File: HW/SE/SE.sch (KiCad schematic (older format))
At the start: 17 parts, among them J1 Conn_01x03_Female, SW1 SW_Push, SW2 Reset, U1 ESP32-WROOM-32, U2 NHD-0420H1Z, U3 NHD-0420H1Z, U4 PCF8574

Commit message: AJustes Dsiplay
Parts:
- removed J1: Conn_01x03_Female, symbol Connector:Conn_01x03_Female
- added C1: 4.7u, symbol Device:C
- added J2: USB_B_Micro, symbol Connector:USB_B_Micro
- added J?: Conn_01x03_Female, symbol Connector:Conn_01x03_Female
- added Q1, Q2: BSS138, Package_TO_SOT_SMD:SOT-23, symbol Transistor_FET:BSS138
- added R6, R7: 10k, symbol Device:R
- added R8: 330, symbol Device:R
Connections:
- net 3.33v: now also Q1.1 (G), Q2.1 (G), R6.2, R7.2
- net 5v: now also C1.1, J2.1 (VBUS), R8.1
- net GND: now reaches D1.1 (K), R5.1, R6.1, R7.1, RV1.3, SW1.2, SW2.2, U1.1 (GND), U1.15 (GND), U1.38 (GND), U1.39 (GND), U2.1 (VSS), U3.1 (VSS), U4.8 (VSS)
- net GND: now also U2.16 (K), U3.16 (K), C1.2, J2.5 (GND), J?.3 (Pin_3)
- net at R4.2, U4.15 (SDA): now also Q2.3 (D); no longer U1.33 (IO21)
- net at U1.34 (RXD0/IO3): now also J?.2 (Pin_2)
- net at U1.35 (TXD0/IO1): now also J?.1 (Pin_1)
- net at R3.2, U4.14 (SCL): now also Q1.3 (D); no longer U1.36 (IO22)
- net at U2.15 (A): now also U3.15 (A), R8.2
- new net SCL: Q1.2 (S), R6.1, U1.36 (IO22)
- new net SDA: Q2.2 (S), R7.1, U1.33 (IO21)
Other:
- moved on the sheet: D1, R1, R2, R3, R4, R5, R6, R7, RV1, SW1, SW2, U1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

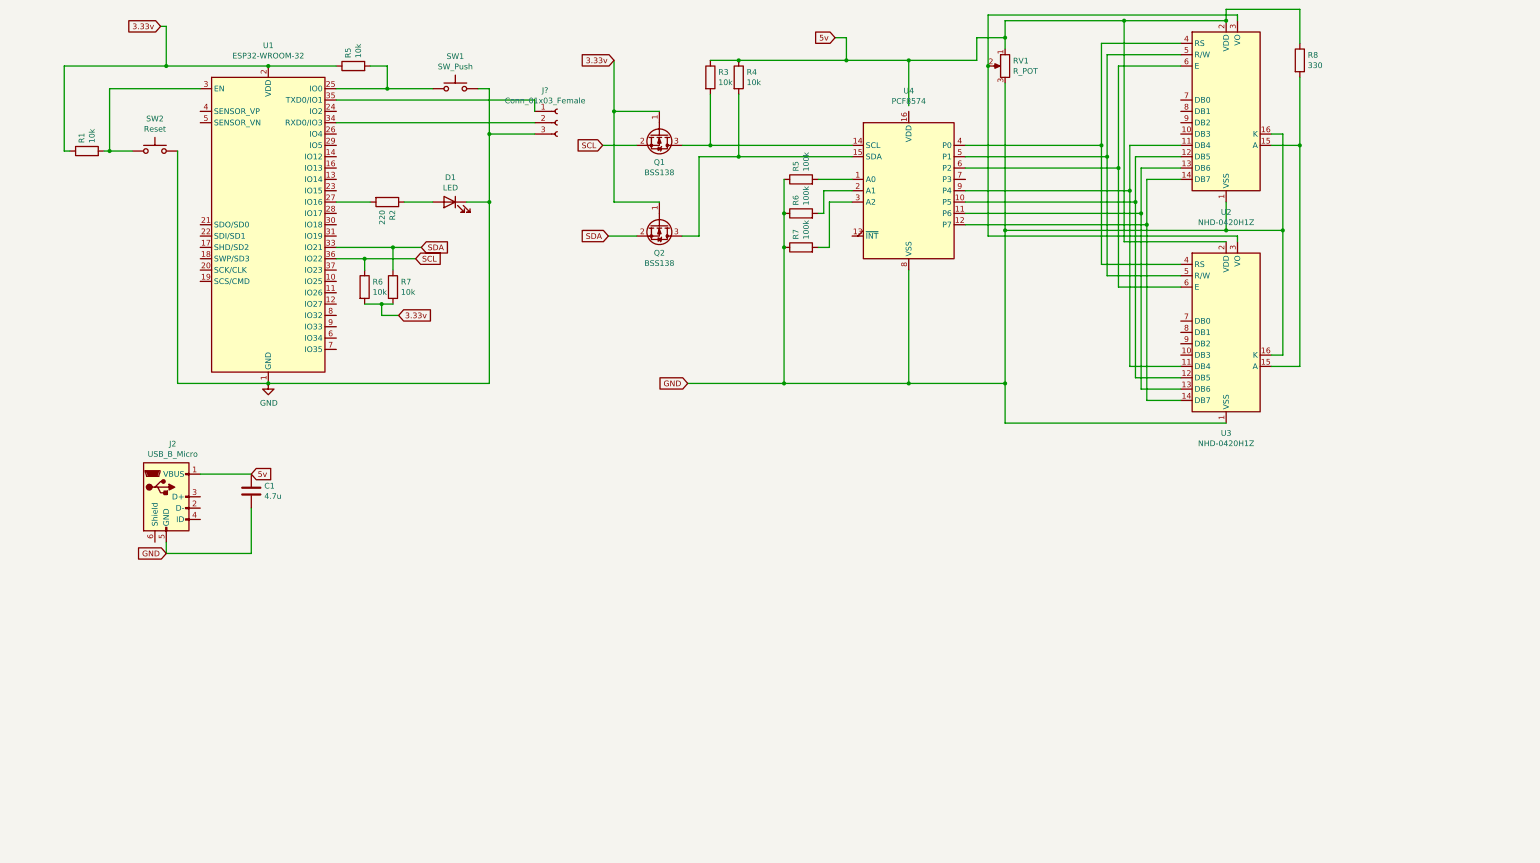
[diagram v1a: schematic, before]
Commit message: Control REle y entrada sensnores
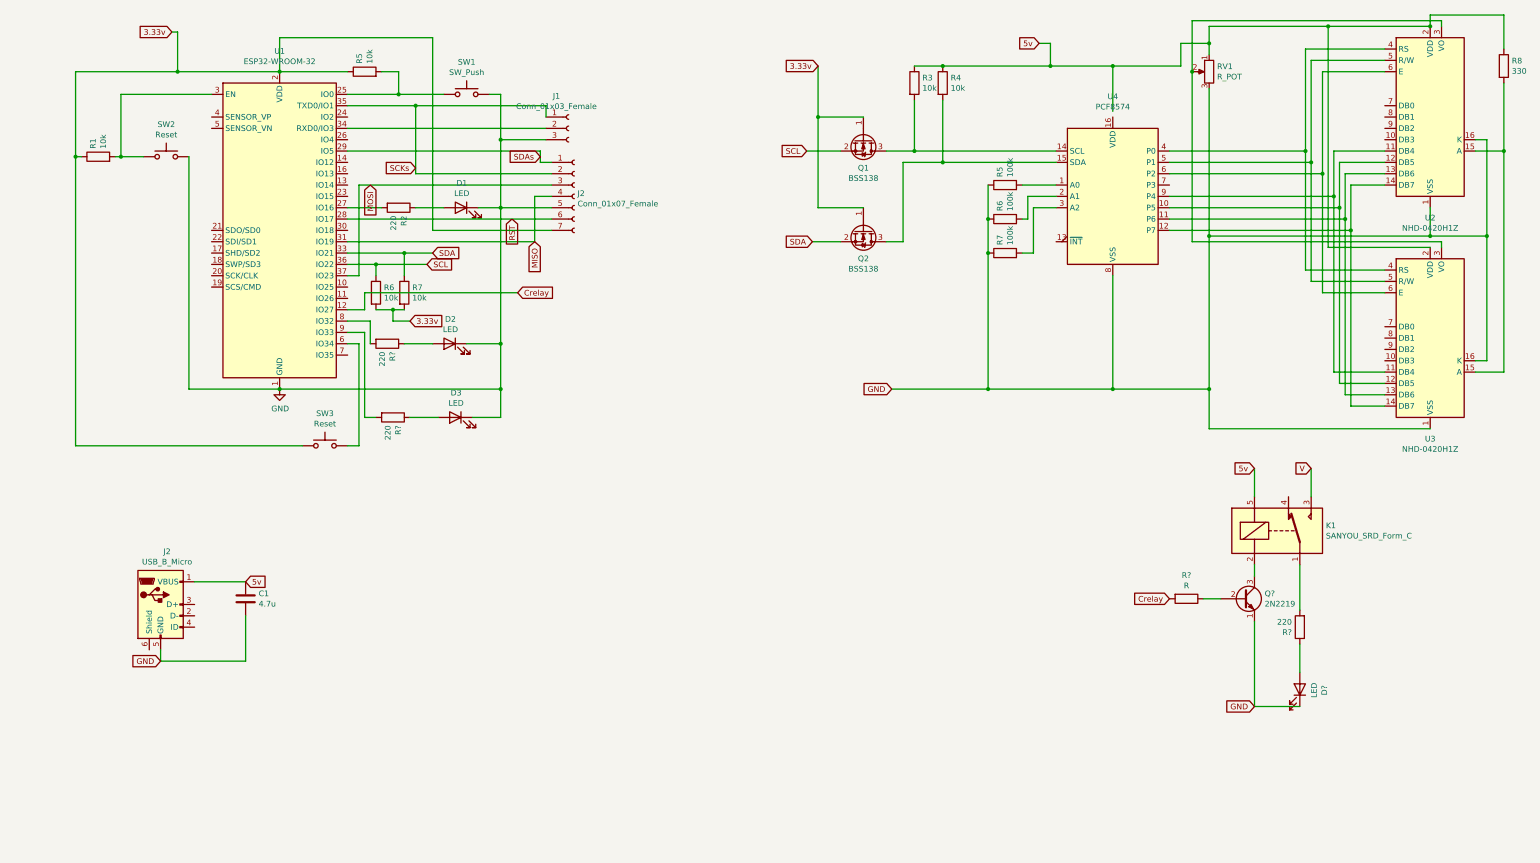
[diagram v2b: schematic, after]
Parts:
- added D2, D3, D?: LED, symbol Device:LED
- added J2: Conn_01x07_Female, symbol Connector:Conn_01x07_Female
- added K1: SANYOU_SRD_Form_C, Relay_THT:Relay_SPDT_SANYOU_SRD_Series_Form_C, symbol Relay:SANYOU_SRD_Form_C
- added Q?: 2N2219, Package_TO_SOT_THT:TO-39-3, symbol Transistor_BJT:2N2219
- added R? (x3): 220, symbol Device:R
- added R?: R, symbol Device:R
- added SW3: Reset, symbol Switch:SW_Push
- gave numbers to parts that had none: 1
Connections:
- net 3.33v: now also J2.7 (Pin_7), SW3.1
- net 5v: now also K1.5
- net GND: now also D2.1 (K), D3.1 (K), D?.1 (K), J2.5 (Pin_5), Q?.1 (E)
- net Crelay: now reaches U1.12 (IO27)
- net Crelay: now also R?.2
- net RST: now reaches U1.28 (IO17)
- net RST: now also J2.6 (Pin_6)
- net SDAs: now reaches U1.29 (IO5)
- net SDAs: now also J2.1 (Pin_1)
- net MISO: now reaches U1.31 (IO19)
- net MISO: now also J2.4 (Pin_4)
- net SCKs: now reaches J1.1 (Pin_1), U1.35 (TXD0/IO1)
- net SCKs: now also J2.2 (Pin_2)
- net MOSI: now reaches U1.37 (IO23)
- net MOSI: now also J2.3 (Pin_3)
- net at U1.6 (IO34): now also SW3.2
- net at U1.8 (IO32): now also R?.2
- net at U1.9 (IO33): now also R?.2
- new net: D2.2 (A), R?.1
- new net: D3.2 (A), R?.1
- new net: K1.1, R?.2
- new net: K1.2, Q?.3 (C)
- new net: Q?.2 (B), R?.1
- new net: D?.2 (A), R?.1
- new net V: K1.3
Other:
- moved on the sheet: C1, D1, J1, J2, Q1, Q2, R1, R2, R3, R4, R5, R6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

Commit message: Ajustes
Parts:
- added D5: 1N4004, Diode_THT:D_DO-41_SOD81_P10.16mm_Horizontal, symbol Diode:1N4004
- gave numbers to parts that had none: 6
- renumbered J2 to J3, R7 to R10, R5 to R13, R6 to R9
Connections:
- net 5v: now also U4.16 (VDD), D5.1 (K)
- net at K1.2, Q3.3 (C): now also D5.2 (A)
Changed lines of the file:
@@
 	12650 2550 10450 2550
 Wire Wire Line
-	10450 2550 10450 1050
-Wire Wire Line
 	12650 650  12650 600
 Wire Wire Line
 	12650 600  10450 600
-Wire Wire Line
-	10450 600  10450 1050
-Connection ~ 10450 1050
 Wire Wire Line
 	12550 2250 12550 2500
@@
 Wire Wire Line
 	9200 1000 9750 1000
-Wire Wire Line
-	9750 1400 9750 1000
 Connection ~ 9750 1000
 Wire Wire Line
@@
 	1000 1800 1200 1800
 $Comp
-L Device:R R5
+L Device:R R13
 U 1 1 62731F59
 P 3150 1050
-F 0 "R5" H 3220 1096 50  0000 L CNN
+F 0 "R13" H 3220 1096 50  0000 L CNN
 F 1 "10k" H 3220 1005 50  0000 L CNN
 F 2 "" V 3080 1050 50  0001 C CNN
@@
 Connection ~ 11500 1850
 $Comp
-L Connector:USB_B_Micro J2
+L Connector:USB_B_Micro J3
 U 1 1 62716DB5
 P 1350 5750
-F 0 "J2" H 1407 6217 50  0000 C CNN
+F 0 "J3" H 1407 6217 50  0000 C CNN
 F 1 "USB_B_Micro" H 1407 6126 50  0000 C CNN
 F 2 "" H 1500 5700 50  0001 C CNN
@@
 $EndComp
 $Comp
-L power:GND #PWR?
+L power:GND #PWR0101
 U 1 1 627211BC
 P 2400 3850
-F 0 "#PWR?" H 2400 3600 50  0001 C CNN
+F 0 "#PWR0101" H 2400 3600 50  0001 C CNN
 F 1 "GND" H 2405 3677 50  0000 C CNN
 F 2 "" H 2400 3850 50  0001 C CNN
@@
 Connection ~ 7150 1450
 $Comp
-L Device:R R6
+L Device:R R9
 U 1 1 628D5267
 P 3250 3000
-F 0 "R6" H 3320 3046 50  0000 L CNN
+F 0 "R9" H 3320 3046 50  0000 L CNN
 F 1 "10k" H 3320 2955 50  0000 L CNN
 F 2 "" V 3180 3000 50  0001 C CNN
@@
 $EndComp
 $Comp
-L Device:R R7
+L Device:R R10
 U 1 1 628D526D
 P 3500 3000
-F 0 "R7" H 3570 3046 50  0000 L CNN
+F 0 "R10" H 3570 3046 50  0000 L CNN
 F 1 "10k" H 3570 2955 50  0000 L CNN
 F 2 "" V 3430 3000 50  0001 C CNN
@@
 $EndComp
 $Comp
-L Device:R R?
+L Device:R R11
 U 1 1 62778922
 P 3350 3450
-F 0 "R?" H 3420 3496 50  0000 L CNN
+F 0 "R11" H 3420 3496 50  0000 L CNN
 F 1 "220" H 3420 3405 50  0000 L CNN
 F 2 "" V 3280 3450 50  0001 C CNN
@@
 $EndComp
 $Comp
-L Device:R R?
+L Device:R R12
 U 1 1 6277F32D
 P 3400 4100
-F 0 "R?" H 3470 4146 50  0000 L CNN
+F 0 "R12" H 3470 4146 50  0000 L CNN
 F 1 "220" H 3470 4055 50  0000 L CNN
 F 2 "" V 3330 4100 50  0001 C CNN
@@
 $EndComp
 $Comp
-L Device:R R?
+L Device:R R14
 U 1 1 628F6BDA
 P 10400 5700
-F 0 "R?" V 10193 5700 50  0000 C CNN
+F 0 "R14" V 10193 5700 50  0000 C CNN
 F 1 "R" V 10284 5700 50  0000 C CNN
 F 2 "" V 10330 5700 50  0001 C CNN
@@
 $EndComp
 $Comp
-L Transistor_BJT:2N2219 Q?
+L Transistor_BJT:2N2219 Q3
 U 1 1 628F7763
 P 10900 5700
-F 0 "Q?" H 11090 5746 50  0000 L CNN
+F 0 "Q3" H 11090 5746 50  0000 L CNN
 F 1 "2N2219" H 11090 5655 50  0000 L CNN
 F 2 "Package_TO_SOT_THT:TO-39-3" H 11100 5625 50  0001 L CIN
@@
 $EndComp
 $Comp
-L Device:LED D?
+L Device:LED D4
 U 1 1 6293854B
 P 11400 6500
-F 0 "D?" H 11393 6717 50  0000 C CNN
+F 0 "D4" H 11393 6717 50  0000 C CNN
 F 1 "LED" H 11393 6626 50  0000 C CNN
 F 2 "" H 11400 6500 50  0001 C CNN
@@
 $EndComp
 $Comp
-L Device:R R?
+L Device:R R15
 U 1 1 62938551
 P 11400 5950
-F 0 "R?" H 11470 5996 50  0000 L CNN
+F 0 "R15" H 11470 5996 50  0000 L CNN
 F 1 "220" H 11470 5905 50  0000 L CNN
 F 2 "" V 11330 5950 50  0001 C CNN
@@
 	10700 5700 10550 5700
 Wire Wire Line
-	11000 4800 11000 4550
+	11000 4800 11000 4750
 Wire Wire Line
 	11500 4550 11500 4800
@@
 Text GLabel 11500 4550 0    50   Input ~ 0
 V
+$Comp
+L Diode:1N4004 D5
+U 1 1 6274A848
+P 10400 5000
+F 0 "D5" V 10354 5080 50  0000 L CNN
+F 1 "1N4004" V 10445 5080 50  0000 L CNN
+F 2 "Diode_THT:D_DO-41_SOD81_P10.16mm_Horizontal" H 10400 4825 50  0001 C CNN
+F 3 "http://www.vishay.com/docs/88503/1n4001.pdf" H 10400 5000 50  0001 C CNN
+	1    10400 5000
+	0    1    1    0
+$EndComp
+Wire Wire Line
+	11000 4750 10400 4750
+Wire Wire Line
+	10400 4750 10400 4850
+Connection ~ 11000 4750
+Wire Wire Line
+	11000 4750 11000 4550
+Wire Wire Line
+	11000 5400 10400 5400
+Wire Wire Line
+	10400 5400 10400 5150
+Connection ~ 11000 5400
+Wire Wire Line
+	9750 1000 9750 1450
+Wire Wire Line
+	10450 600  10450 1050
+Connection ~ 10450 1050
+Wire Wire Line
+	10450 1050 10450 2550
 $EndSCHEMATC

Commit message: Primer diseño fuente
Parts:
- removed C1: 4.7u, symbol Device:C
- removed J3: USB_B_Micro, symbol Connector:USB_B_Micro
- added C?: 1000u, symbol Device:CP1
- added C?: 100u, symbol Device:CP1
- added C? (x3): 100n, symbol Device:C
- added C? (x2): 22u, symbol Device:CP1
- added D?: MBR1020VL, Diode_SMD:D_SOD-123F, symbol Diode:MBR1020VL
- added F?: Fuse, symbol Device:Fuse
- added J3, J?: Conn_01x02_Female, symbol Connector:Conn_01x02_Female
- added Q?: DMG3414U, Package_TO_SOT_SMD:SOT-23, symbol Transistor_FET:DMG3414U
- added R?: R, symbol Device:R
- added SW?: SW_DPST_x2, symbol Switch:SW_DPST_x2
- added U?: AMS1117-3.3, Package_TO_SOT_SMD:SOT-223-3_TabPin2, symbol Regulator_Linear:AMS1117-3.3
- added U?: AMS1117-5.0, Package_TO_SOT_SMD:SOT-223-3_TabPin2, symbol Regulator_Linear:AMS1117-5.0
- SW2: value Reset -> ResetP
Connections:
- net 5v: now also C?.1, C?.1, C?.1, U?.2 (VO), U?.3 (VI)
- net GND: now also C?.2, C?.2, C?.2, C?.2, C?.2, C?.2, C?.2, J3.2 (Pin_2), J?.2 (Pin_2), R?.2, U?.1 (GND), U?.1 (GND)
- net SCKs: now also U1.16 (IO13); no longer J1.1 (Pin_1), U1.35 (TXD0/IO1)
- net 12v: now reaches K1.4
- net 12v: now also C?.1, C?.1, SW?.2 (B), U?.3 (VI)
- net V: no longer names the net of K1.3
- new net: J1.1 (Pin_1), U1.35 (TXD0/IO1)
- new net: F?.1, J3.1 (Pin_1)
- new net: D?.1 (K), Q?.2 (S), SW?.1 (A)
- new net: D?.2 (A), F?.2, Q?.1 (G), R?.1
- new net 3.3v: C?.1, C?.1, U?.2 (VO)
- new net Vbat: J?.1 (Pin_1), Q?.3 (D)

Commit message: Esquematico Completo
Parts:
- removed Q3: 2N2219, Package_TO_SOT_THT:TO-39-3, symbol Transistor_BJT:2N2219
- removed R15: 220, symbol Device:R
- added BZ1: Buzzer, symbol Device:Buzzer
- added C? (x3): 10u, symbol Device:C
- added J5: Conn_01x02_Female, symbol Connector:Conn_01x02_Female
- added Q1: BC548, Package_TO_SOT_THT:TO-92_Inline, symbol Transistor_BJT:BC548
- R14: value R -> 5.6k
- gave numbers to parts that had none: 3
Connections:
- net 3.33v: now also C?.1
- net 5v: now also BZ1.1 (-)
- net Crelay: now also D4.2 (A); no longer R14.2
- net GND: now also C?.1, C?.2, J5.2 (Pin_2), Q1.3 (E); no longer D4.1 (K)
- net at R13.2, SW1.1, U1.25 (IO0): now also C?.2
- net at R1.2, SW2.1, U1.3 (EN): now also C?.1
- net at SW3.2, U1.6 (IO34): now also C?.2
- net at D5.2 (A), K1.2: now also BZ1.2 (+), Q1.1 (C)
- net at K1.1: now also J5.1 (Pin_1)
- net at R14.1: now also Q1.2 (B)
- new net: D4.1 (K), R14.2
- no-connect marks 0 -> 9
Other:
- moved on the sheet: D4, D5, K1, R14

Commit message: A
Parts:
- gave numbers to parts that had none: 15
- renumbered Q1 to Q3
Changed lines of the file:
@@
 	3000 1950 4800 1950
 $Comp
-L Transistor_BJT:BC548 Q1
+L Transistor_BJT:BC548 Q3
 U 1 1 62B6F2E3
 P 10900 5450
-F 0 "Q1" H 11091 5496 50  0000 L CNN
+F 0 "Q3" H 11091 5496 50  0000 L CNN
 F 1 "BC548" H 11091 5405 50  0000 L CNN
 F 2 "Package_TO_SOT_THT:TO-92_Inline" H 11100 5375 50  0001 L CIN
@@
 	2400 5700 2300 5700
 $Comp
-L Device:R R?
+L Device:R R15
 U 1 1 62A82EEA
 P 2300 5950
-F 0 "R?" H 2370 5996 50  0000 L CNN
+F 0 "R15" H 2370 5996 50  0000 L CNN
 F 1 "R" H 2370 5905 50  0000 L CNN
 F 2 "" V 2230 5950 50  0001 C CNN
@@
 $EndComp
 $Comp
-L Diode:MBR1020VL D?
+L Diode:MBR1020VL D6
 U 1 1 62A4C6B4
 P 2550 5700
-F 0 "D?" H 2550 5916 50  0000 C CNN
+F 0 "D6" H 2550 5916 50  0000 C CNN
 F 1 "MBR1020VL" H 2550 5825 50  0000 C CNN
 F 2 "Diode_SMD:D_SOD-123F" H 2550 5525 50  0001 C CNN
@@
 $EndComp
 $Comp
-L Transistor_FET:DMG3414U Q?
+L Transistor_FET:DMG3414U Q3
 U 1 1 62A48C01
 P 2750 5300
-F 0 "Q?" H 2954 5346 50  0000 L CNN
+F 0 "Q3" H 2954 5346 50  0000 L CNN
 F 1 "DMG3414U" H 2954 5255 50  0000 L CNN
 F 2 "Package_TO_SOT_SMD:SOT-23" H 2950 5225 50  0001 L CIN
@@
 	1250 5700 1100 5700
 $Comp
-L Device:Fuse F?
+L Device:Fuse F1
 U 1 1 62A27429
 P 1400 5700
-F 0 "F?" H 1460 5746 50  0000 L CNN
+F 0 "F1" H 1460 5746 50  0000 L CNN
 F 1 "Fuse" H 1460 5655 50  0000 L CNN
 F 2 "" V 1330 5700 50  0001 C CNN
@@
 	6500 5700 6300 5700
 $Comp
-L Device:C C?
+L Device:C C10
 U 1 1 6290AFBF
 P 7750 6000
-F 0 "C?" H 7865 6046 50  0000 L CNN
+F 0 "C10" H 7865 6046 50  0000 L CNN
 F 1 "100n" H 7865 5955 50  0000 L CNN
 F 2 "" H 7788 5850 50  0001 C CNN
@@
 $EndComp
 $Comp
-L Device:CP1 C?
+L Device:CP1 C9
 U 1 1 6290AFB9
 P 7400 6000
-F 0 "C?" H 7515 6046 50  0000 L CNN
+F 0 "C9" H 7515 6046 50  0000 L CNN
 F 1 "22u" H 7515 5955 50  0000 L CNN
 F 2 "" H 7400 6000 50  0001 C CNN
@@
 $EndComp
 $Comp
-L Device:C C?
+L Device:C C8
 U 1 1 628EF7EF
 P 6300 6000
-F 0 "C?" H 6415 6046 50  0000 L CNN
+F 0 "C8" H 6415 6046 50  0000 L CNN
 F 1 "100n" H 6415 5955 50  0000 L CNN
 F 2 "" H 6338 5850 50  0001 C CNN
@@
 $EndComp
 $Comp
-L Device:CP1 C?
+L Device:CP1 C7
 U 1 1 628EEA1D
 P 5950 6000
-F 0 "C?" H 6065 6046 50  0000 L CNN
+F 0 "C7" H 6065 6046 50  0000 L CNN
 F 1 "22u" H 6065 5955 50  0000 L CNN
 F 2 "" H 5950 6000 50  0001 C CNN
@@
 $EndComp
 $Comp
-L Switch:SW_DPST_x2 SW?
+L Switch:SW_DPST_x2 SW4
 U 1 1 628CD103
 P 3300 5700
-F 0 "SW?" H 3300 5935 50  0000 C CNN
+F 0 "SW4" H 3300 5935 50  0000 C CNN
 F 1 "SW_DPST_x2" H 3300 5844 50  0000 C CNN
 F 2 "" H 3300 5700 50  0001 C CNN
@@
 	5450 5850 5450 5700
 $Comp
-L Device:C C?
+L Device:C C4
 U 1 1 628291A6
 P 4150 6000
-F 0 "C?" H 4265 6046 50  0000 L CNN
+F 0 "C4" H 4265 6046 50  0000 L CNN
 F 1 "100n" H 4265 5955 50  0000 L CNN
 F 2 "" H 4188 5850 50  0001 C CNN
@@
 $EndComp
 $Comp
-L Device:CP1 C?
+L Device:CP1 C6
 U 1 1 62828B3C
 P 5450 6000
-F 0 "C?" H 5565 6046 50  0000 L CNN
+F 0 "C6" H 5565 6046 50  0000 L CNN
 F 1 "100u" H 5565 5955 50  0000 L CNN
 F 2 "" H 5450 6000 50  0001 C CNN
@@
 $EndComp
 $Comp
-L Device:CP1 C?
+L Device:CP1 C5
 U 1 1 62827CE5
 P 4550 6000
-F 0 "C?" H 4665 6046 50  0000 L CNN
+F 0 "C5" H 4665 6046 50  0000 L CNN
 F 1 "1000u" H 4665 5955 50  0000 L CNN
 F 2 "" H 4550 6000 50  0001 C CNN
@@
 $EndComp
 $Comp
-L Device:C C?
+L Device:C C2
 U 1 1 62C0D630
 P 2800 4600
-F 0 "C?" V 3052 4600 50  0000 C CNN
+F 0 "C2" V 3052 4600 50  0000 C CNN
 F 1 "10u" V 2961 4600 50  0000 C CNN
 F 2 "" H 2838 4450 50  0001 C CNN
@@
 $EndComp
 $Comp
-L Device:C C?
+L Device:C C1
 U 1 1 62C0E2EB
 P 1400 2050
-F 0 "C?" V 1652 2050 50  0000 C CNN
+F 0 "C1" V 1652 2050 50  0000 C CNN
 F 1 "10u" V 1561 2050 50  0000 C CNN
 F 2 "" H 1438 1900 50  0001 C CNN
@@
 	1000 2050 1000 1800
 $Comp
-L Device:C C?
+L Device:C C3
 U 1 1 62C89994
 P 4050 800
-F 0 "C?" V 4302 800 50  0000 C CNN
+F 0 "C3" V 4302 800 50  0000 C CNN
 F 1 "10u" V 4211 800 50  0000 C CNN
 F 2 "" H 4088 650 50  0001 C CNN

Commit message: h
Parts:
- removed BZ1: Buzzer, symbol Device:Buzzer
- removed D5: 1N4004, Diode_THT:D_DO-41_SOD81_P10.16mm_Horizontal, symbol Diode:1N4004
- removed Q3: DMG3414U, Package_TO_SOT_SMD:SOT-23, symbol Transistor_FET:DMG3414U
- removed SW4: SW_DPST_x2, symbol Switch:SW_DPST_x2
- added D5: 1N4148W, Diode_SMD:D_SOD-123, symbol Diode:1N4148W
- added D7, D8: LED, symbol Device:LED
- added R16, R17: 1k, symbol Device:R
- added SW4: SW_DPDT_x2, symbol Switch:SW_DPDT_x2
- added U7: DMG3415U-7, LIB:SOT95P240X105-3N, symbol DMG3415U-7:DMG3415U-7
- C5: value 1000u -> 100u
- J1: footprint (none) -> Connector_PinSocket_2.54mm:PinSocket_1x03_P2.54mm_Horizontal
- J2: footprint (none) -> Connector_Molex:Molex_Micro-Latch_53254-0770_1x07_P2.00mm_Horizontal
- J3, J4, J5: footprint (none) -> Connector_Molex:Molex_Micro-Latch_53254-0270_1x02_P2.00mm_Horizontal
- R15: value R -> 100k
- RV1: value R_POT -> 10k
- U4: footprint (none) -> LIB:PCF8574ADWR_DW16
- renumbered Q3 to Q4
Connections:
- net 12v: now also R17.1, SW4.3 (C)
- net 5v: now also D5.1 (K)
- net GND: now also D7.1 (K), D8.1 (K)
- net Vbat: now also U7.3 (D)
- net at K1.2, Q4.1 (C): now also D5.2 (A)
- net at D6.1 (K): now also SW4.2 (B), U7.2 (S)
- net at D6.2 (A), F1.2, R15.1: now also R16.1, U7.1 (G)
- new net: D8.2 (A), R17.2
- new net: D7.2 (A), R16.2
- no-connect marks 9 -> 27
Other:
- moved on the sheet: C10, C4, C5, C6, C7, C8, C9, D6, F1, J3, J4, R15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

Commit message: F
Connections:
- net Crelay: now also R14.1; no longer D4.2 (A)
- net GND: now also D4.1 (K)
- net at Q4.2 (B): now also D4.2 (A), R14.2; no longer R14.1
- no-connect marks 27 -> 28
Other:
- moved on the sheet: D4, R14
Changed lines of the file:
@@
 $EndComp
-Wire Wire Line
-	9700 5450 10000 5450
-Wire Wire Line
-	10300 5450 10350 5450
-Wire Wire Line
-	10700 5450 10650 5450
 Wire Wire Line
 	11400 5800 11400 6400
@@
 L Device:LED D4
 U 1 1 6293854B
-P 10150 5450
-F 0 "D4" H 10143 5667 50  0000 C CNN
-F 1 "LED" H 10143 5576 50  0000 C CNN
-F 2 "" H 10150 5450 50  0001 C CNN
-F 3 "~" H 10150 5450 50  0001 C CNN
-	1    10150 5450
-	-1   0    0    -1
+P 10600 6050
+F 0 "D4" H 10593 6267 50  0000 C CNN
+F 1 "LED" H 10593 6176 50  0000 C CNN
+F 2 "" H 10600 6050 50  0001 C CNN
+F 3 "~" H 10600 6050 50  0001 C CNN
+	1    10600 6050
+	0    1    -1   0
 $EndComp
 Wire Wire Line
@@
 Text GLabel 11400 6400 2    50   Input ~ 0
 GND
-Text GLabel 9700 5450 0    50   Input ~ 0
+Text GLabel 9650 5450 0    50   Input ~ 0
 Crelay
 Text GLabel 11000 4300 0    50   Input ~ 0
@@
 L Device:R R14
 U 1 1 628F6BDA
-P 10500 5450
-F 0 "R14" V 10293 5450 50  0000 C CNN
-F 1 "5.6k" V 10384 5450 50  0000 C CNN
-F 2 "" V 10430 5450 50  0001 C CNN
-F 3 "~" H 10500 5450 50  0001 C CNN
-	1    10500 5450
-	0    1    1    0
+P 10250 5450
+F 0 "R14" V 10043 5450 50  0000 C CNN
+F 1 "5.6k" V 10134 5450 50  0000 C CNN
+F 2 "" V 10180 5450 50  0001 C CNN
+F 3 "~" H 10250 5450 50  0001 C CNN
+	1    10250 5450
+	0    -1   -1   0
 $EndComp
 Connection ~ 11000 5150
@@
 Wire Wire Line
 	1800 5850 2850 5850
+Wire Wire Line
+	10600 5450 10700 5450
+Wire Wire Line
+	10600 6200 10600 6400
+Wire Wire Line
+	10600 6400 11000 6400
+Connection ~ 11000 6400
+NoConn ~ 10250 2050
+Wire Wire Line
+	10600 5450 10400 5450
+Connection ~ 10600 5450
+Wire Wire Line
+	9650 5450 10100 5450
+Wire Wire Line
+	10600 5450 10600 5900
 $EndSCHEMATC
